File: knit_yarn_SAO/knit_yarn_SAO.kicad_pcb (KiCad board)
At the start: 2 copper layers, 33.8 x 36.1 mm, 14 parts, among them SW1 SW_SPST

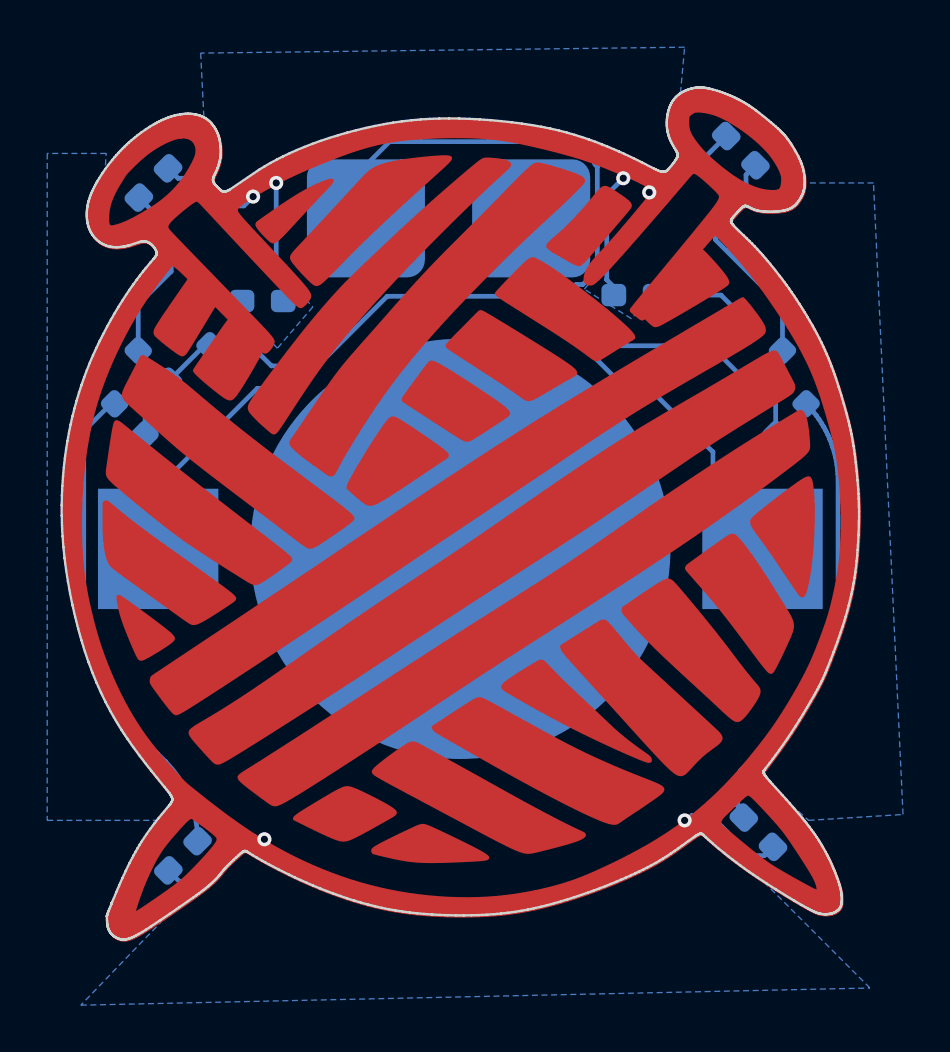
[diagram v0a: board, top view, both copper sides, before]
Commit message: SAO connected and errors checked
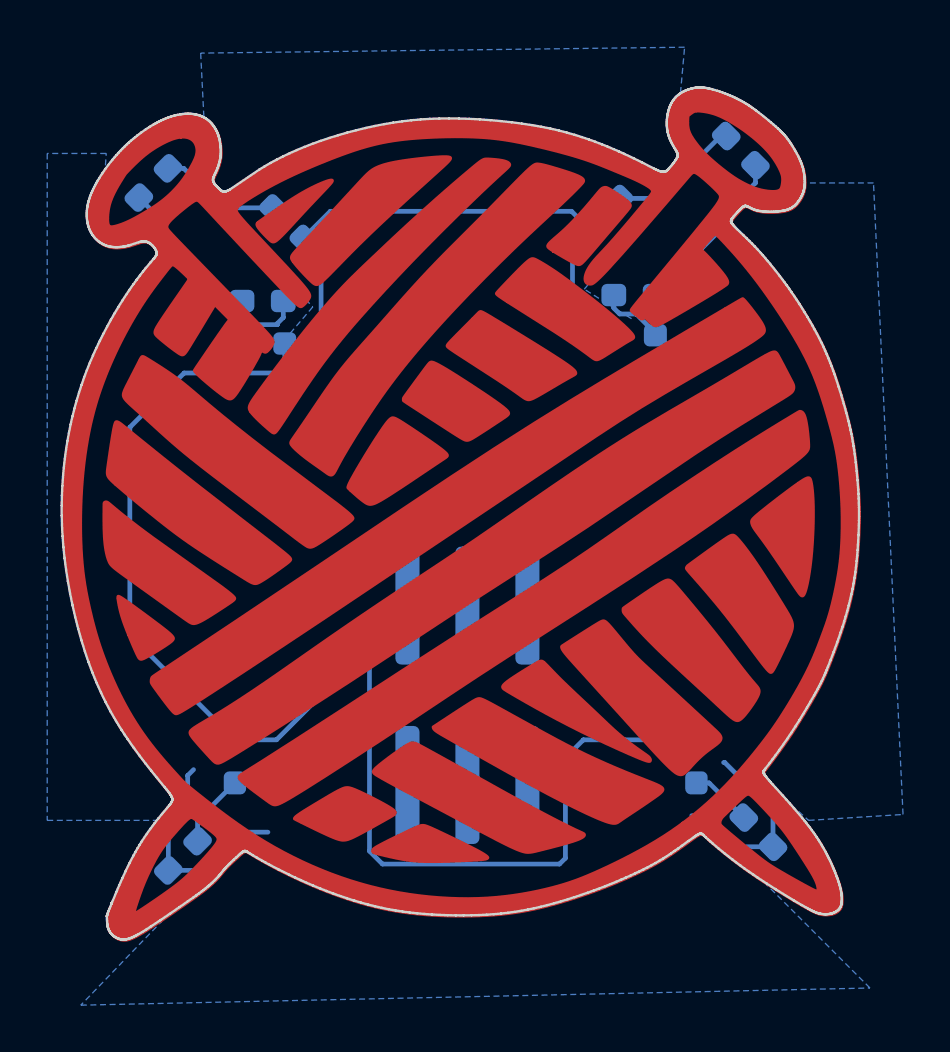
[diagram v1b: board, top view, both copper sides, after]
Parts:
- removed BT1: Battery_Cell, Battery:BatteryHolder_Keystone_3002_1x2032
- removed SW1: SW_SPST, Boris_Custom:brooch_SW_20mm
- added J1: Conn_02x03_Odd_Even, Connector_IDC:IDC-Header_2x03_P2.54mm_Vertical_SMD, B.Cu at (100.3, 97.2)
- moved R2 15.2 mm to (90.5, 100.0), turned to -90 degrees
- moved R1 15.0 mm to (110.0, 100.0), turned to -90 degrees
- moved R3 9.45 mm to (106.1, 76.8)
- moved R4 8.31 mm to (92.7, 77.2)
- moved R5 3.91 mm to (107.3, 82.0), turned to 0 degrees
- moved R6 2.95 mm to (91.7, 82.3), turned to 180 degrees
- turned D3 to 135 degrees
- turned D4 to 45 degrees
- turned D5 to 180 degrees
- turned D6 to 0 degrees
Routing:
- net Net-(BT1-+): track 40.5 -> 0.00 mm
- net +3V0: track 49.9 -> 85.8 mm
- net Net-(D2-A): track 20.4 -> 3.12 mm
- net Net-(D1-A): track 19.1 -> 2.61 mm
- net Net-(D3-A): track 9.89 -> 5.63 mm
- net GND: track 29.5 -> 32.1 mm, vias 6 -> 0
- net Net-(D4-A): track 7.63 -> 5.25 mm
- net Net-(D5-A): track 4.00 -> 2.84 mm

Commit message: added the question
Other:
- board text added: "2025/12/03"
- board text added: "What if you don't stop?"
- board text removed: "2025/12/02"
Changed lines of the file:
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@@
 		)
 	)
-	(gr_text "2025/12/02"
+	(gr_text "2025/12/03"
 		(at 104.5 75.35 0)
 		(layer "B.SilkS")
@@
 		)
 	)
+	(gr_text "What if you \ndon't stop?"
+		(at 99.35 81.95 0)
+		(layer "B.SilkS")
+		(effects
+			(font
+				(size 1 1)
+				(thickness 0.2)
+				(bold yes)
+			)
+			(justify bottom mirror)
+		)
+	)
